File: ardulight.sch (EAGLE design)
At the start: 21 parts, among them U1 ATMEGA32U4QFN2, Y1 16MHz

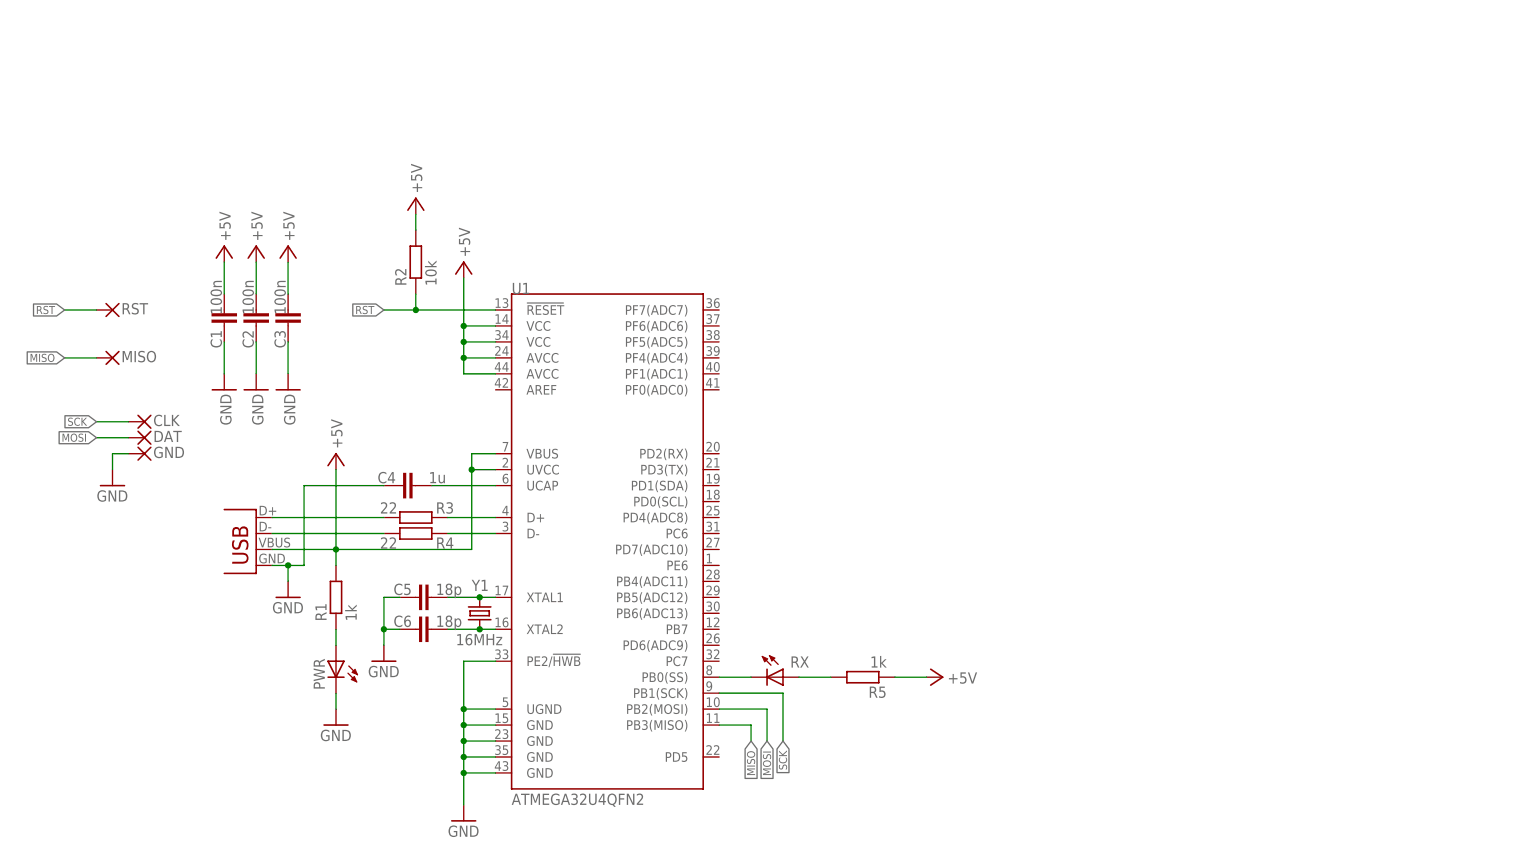
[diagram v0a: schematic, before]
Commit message: add vcc to isp
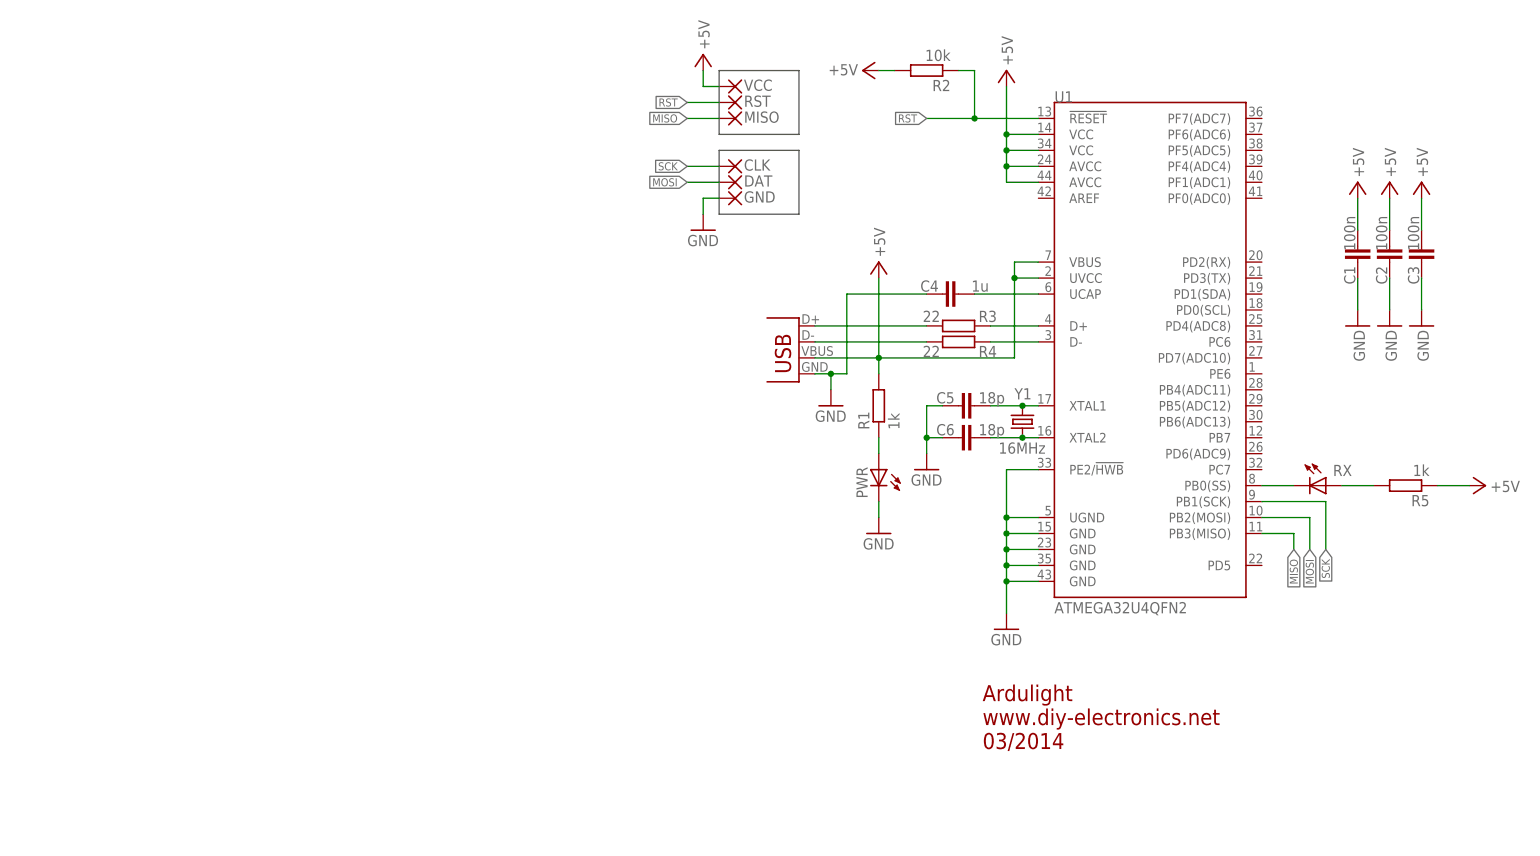
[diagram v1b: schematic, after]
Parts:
- added VCC: (no value), wirepad:SMD2
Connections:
- net +5V: now also VCC.P
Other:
- note added: "03/2014"
- note added: "Ardulight"
- note added: "www.diy-electronics.net"
- moved on the sheet: C1, C2, C3, C4, C5, C6, CLK, DAT, GND, MISO, PWR, R1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

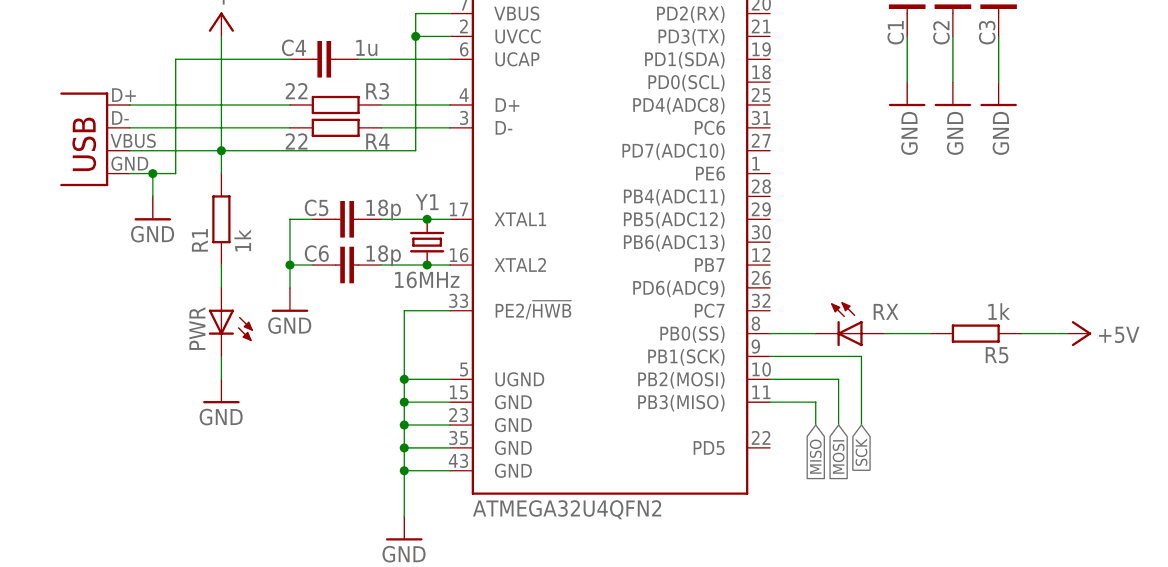
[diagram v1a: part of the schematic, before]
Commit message: more information regarding assembly etc
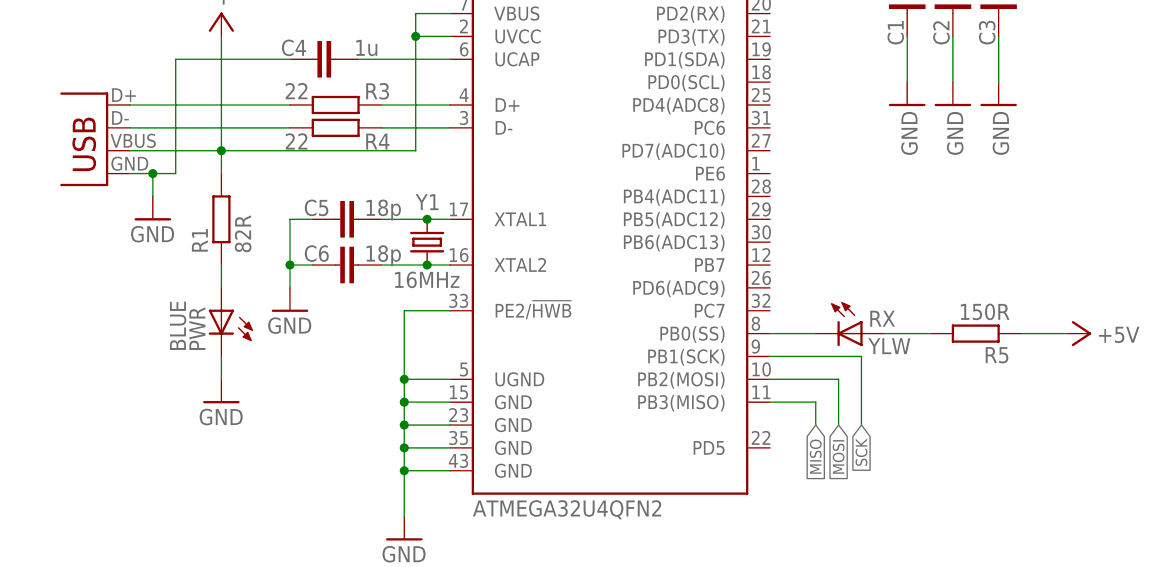
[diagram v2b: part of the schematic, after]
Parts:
- PWR: value (none) -> BLUE
- R1: value 1k -> 82R
- R5: value 1k -> 150R
- RX: value (none) -> YLW
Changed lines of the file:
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@@
 <?xml version="1.0" encoding="utf-8"?>
 <!DOCTYPE eagle SYSTEM "eagle.dtd">
-<eagle version="6.5.0">
+<eagle version="7.1.0">
 <drawing>
 <settings>
@@
 <part name="R4" library="rcl" deviceset="R-EU_" device="R0603" value="22"/>
 <part name="P+3" library="supply1" deviceset="+5V" device=""/>
-<part name="PWR" library="adafruit" deviceset="LED" device="CHIPLED_0603"/>
-<part name="R1" library="rcl" deviceset="R-EU_" device="R0603" value="1k"/>
+<part name="PWR" library="adafruit" deviceset="LED" device="CHIPLED_0603" value="BLUE"/>
+<part name="R1" library="rcl" deviceset="R-EU_" device="R0603" value="82R"/>
 <part name="GND3" library="supply1" deviceset="GND" device=""/>
 <part name="GND4" library="supply1" deviceset="GND" device=""/>
@@
 <part name="GND6" library="supply1" deviceset="GND" device=""/>
 <part name="GND7" library="supply1" deviceset="GND" device=""/>
-<part name="RX" library="adafruit" deviceset="LED" device="CHIPLED_0603"/>
-<part name="R5" library="rcl" deviceset="R-EU_" device="R0603" value="1k"/>
+<part name="RX" library="adafruit" deviceset="LED" device="CHIPLED_0603" value="YLW"/>
+<part name="R5" library="rcl" deviceset="R-EU_" device="R0603" value="150R"/>
 <part name="P+7" library="supply1" deviceset="+5V" device=""/>
 <part name="GND" library="wirepad" deviceset="SMD5" device=""/>
@@
 </instance>
 <instance part="RX" gate="G$1" x="142.24" y="53.34" smashed="yes" rot="R270">
-<attribute name="NAME" x="143.383" y="54.864" size="1.778" layer="95"/>
-<attribute name="VALUE" x="137.668" y="47.625" size="1.778" layer="96"/>
+<attribute name="NAME" x="143.002" y="54.102" size="1.778" layer="95"/>
+<attribute name="VALUE" x="143.002" y="51.054" size="1.778" layer="96"/>
 </instance>
 <instance part="R5" gate="G$1" x="154.94" y="53.34" rot="R180"/>
@@
 </sheet>
 </sheets>
+<errors>
+</errors>
 </schematic>
 </drawing>
